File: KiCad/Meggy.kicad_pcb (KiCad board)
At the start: 4 copper layers, 17.4 x 54 mm, 19 parts, among them J1 USB_B_Micro, J2 Conn_01x03, Q1 DMP2305U-7, Q2 DMP2305U-7, U1 ROM-socket-42pin, U2 AT90USB1286-MU, U3 M29F160F, X1 Standard_Clock_Oscillators_XT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

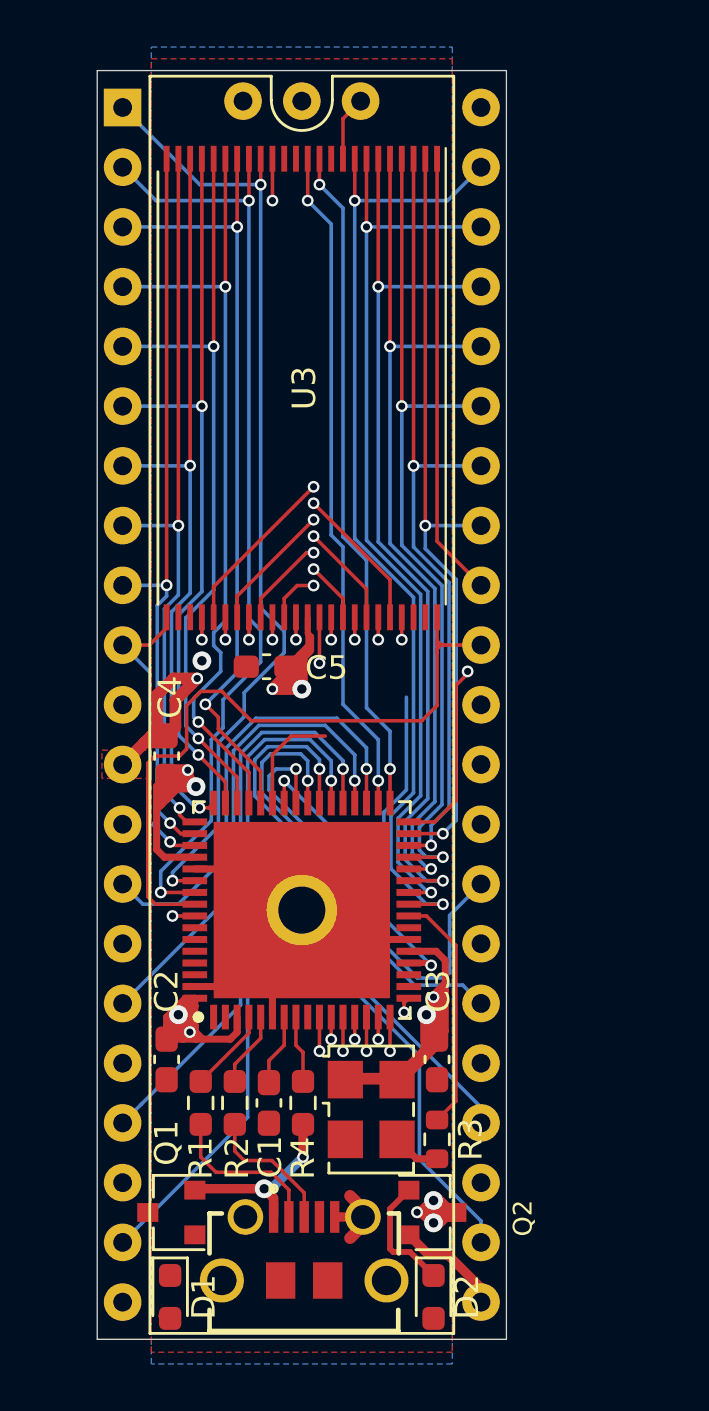
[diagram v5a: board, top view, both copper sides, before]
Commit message: Add circuit for controlling Flash-OE signal
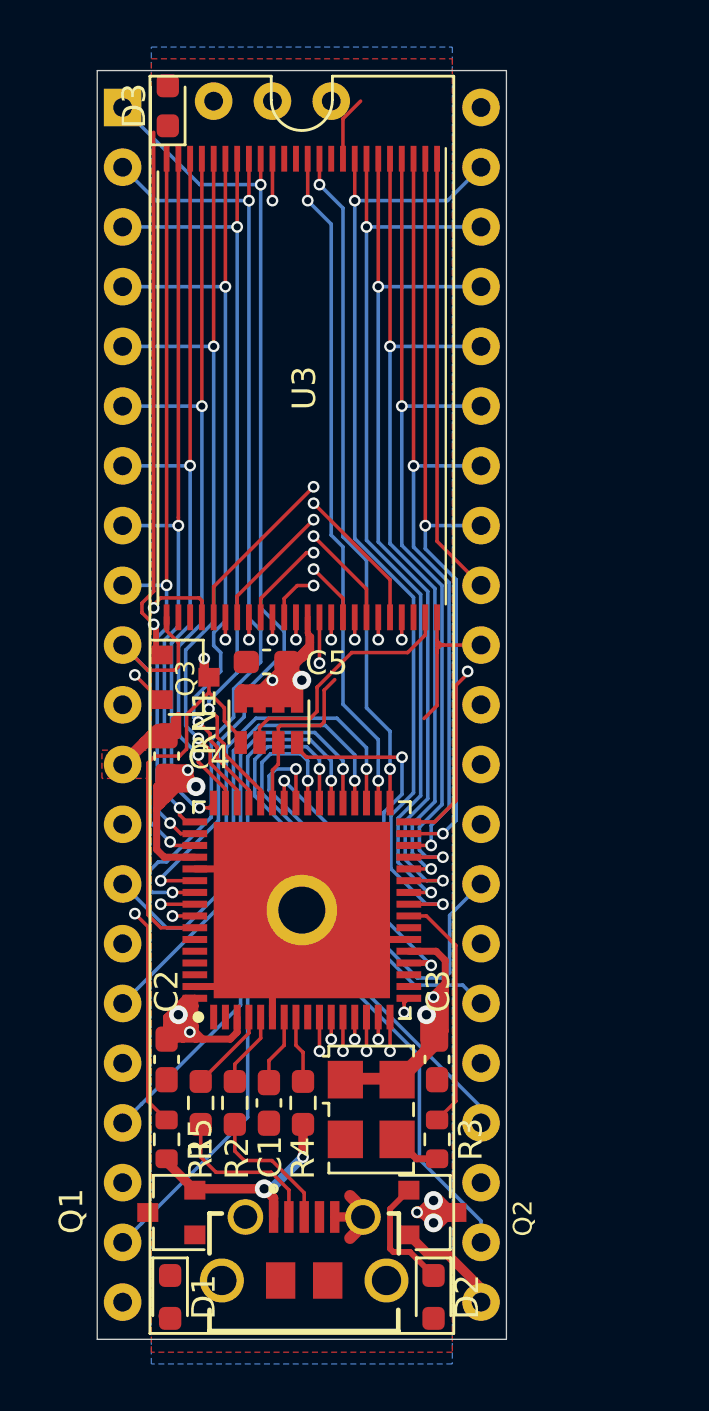
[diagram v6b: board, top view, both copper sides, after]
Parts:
- added D3: MMDL6050T1G, Meggy:D_0603_1608Metric_Pad_0.975x0.95mm_HandSolder, F.Cu at (126.3, 58.8)
- added Q3: DMP2305U-7, Package_TO_SOT_SMD:SOT-23, F.Cu at (127.0, 83.1)
- added R5: 10k, Resistor_SMD:R_0603_1608Metric, F.Cu at (126.2, 102.8)
- added RN1: 10k, Meggy:RESCAF80P320X160X60-8N, F.Cu at (130.6, 85.0)
- moved J2 1.25 mm to (130.8, 58.6)
- moved C5 0.20 mm to (130.5, 82.5)
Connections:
- net Net-(C1-Pad1) renamed /UCAP
- U2 pad 58: PF3 -> OE_FLASH
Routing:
- net Net-(D3-Pad1): track 0.00 -> 45.1 mm, vias 0 -> 2
- net OE_FLASH: track 0.95 -> 24.3 mm, vias 1 -> 2
- net BYTE: track 0.00 -> 10.7 mm
- net BOARD_5V: track 72.6 -> 81.9 mm
- net OE_SOCKET: track 0.00 -> 9.23 mm, vias 0 -> 1
- net GND: track 35.0 -> 31.1 mm, vias 2 -> 0
- net A0: track 12.9 -> 15.8 mm
- net HWB: track 4.63 -> 7.35 mm
- net RESET: track 13.6 -> 15.8 mm, vias 1 -> 2
- net VBUS_5V: track 7.73 -> 9.57 mm
- net D0: track 41.5 -> 43.0 mm
- net A17: track 40.6 -> 41.4 mm
- net A18: track 41.3 -> 42.0 mm
- net A16: track 29.6 -> 29.3 mm, vias 0 -> 1

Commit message: Add 10k pull-up resistor network for RY-BY, WE, RST and A19 signals
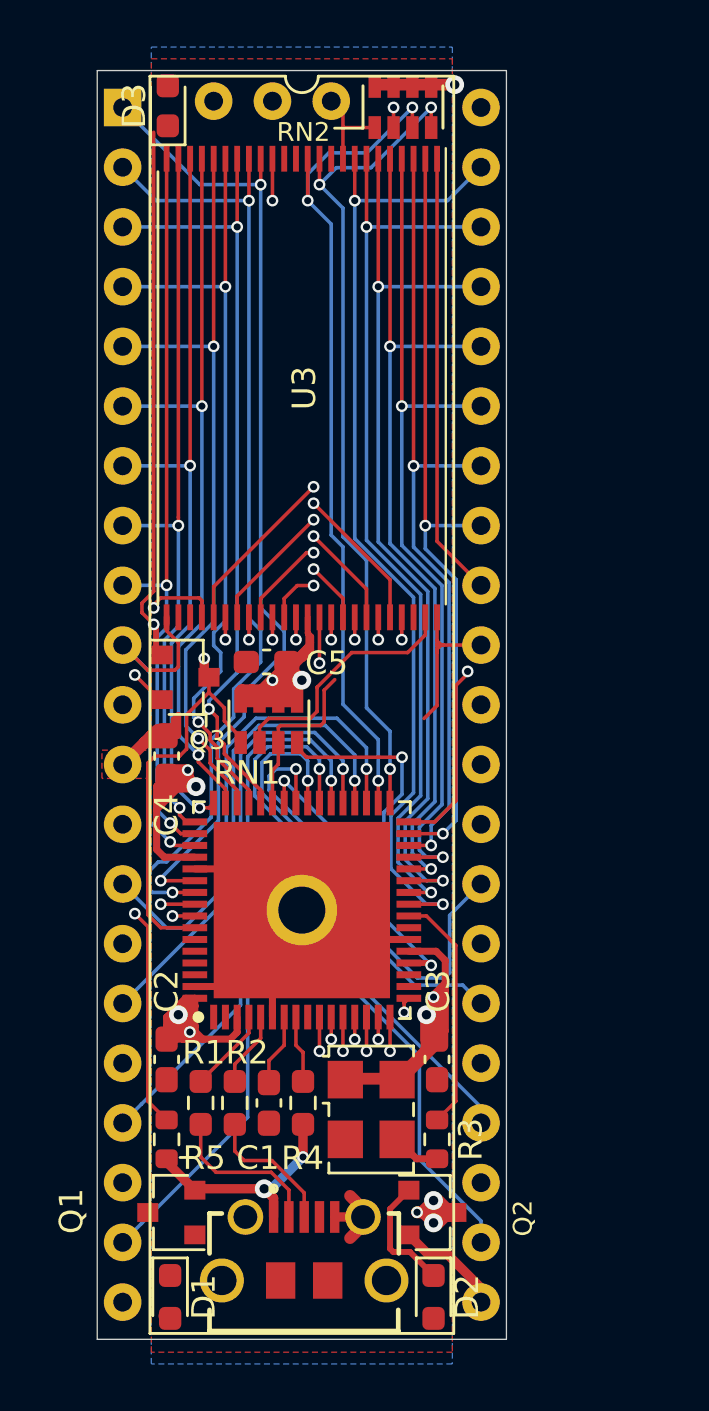
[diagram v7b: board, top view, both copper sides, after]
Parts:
- added RN2: 10k, Meggy:RESCAF80P320X160X60-8N, F.Cu at (136.3, 58.9)
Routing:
- net RY-BY: track 35.5 -> 43.1 mm, vias 2 -> 3
- net RST: track 28.6 -> 36.2 mm, vias 2 -> 3
- net WE: track 28.6 -> 35.6 mm, vias 2 -> 3
- net BOARD_5V: track 81.9 -> 85.4 mm, vias 11 -> 12
- net A19: track 2.76 -> 4.02 mm

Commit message: Fix footprint for diode D3 and silkscreen fixes
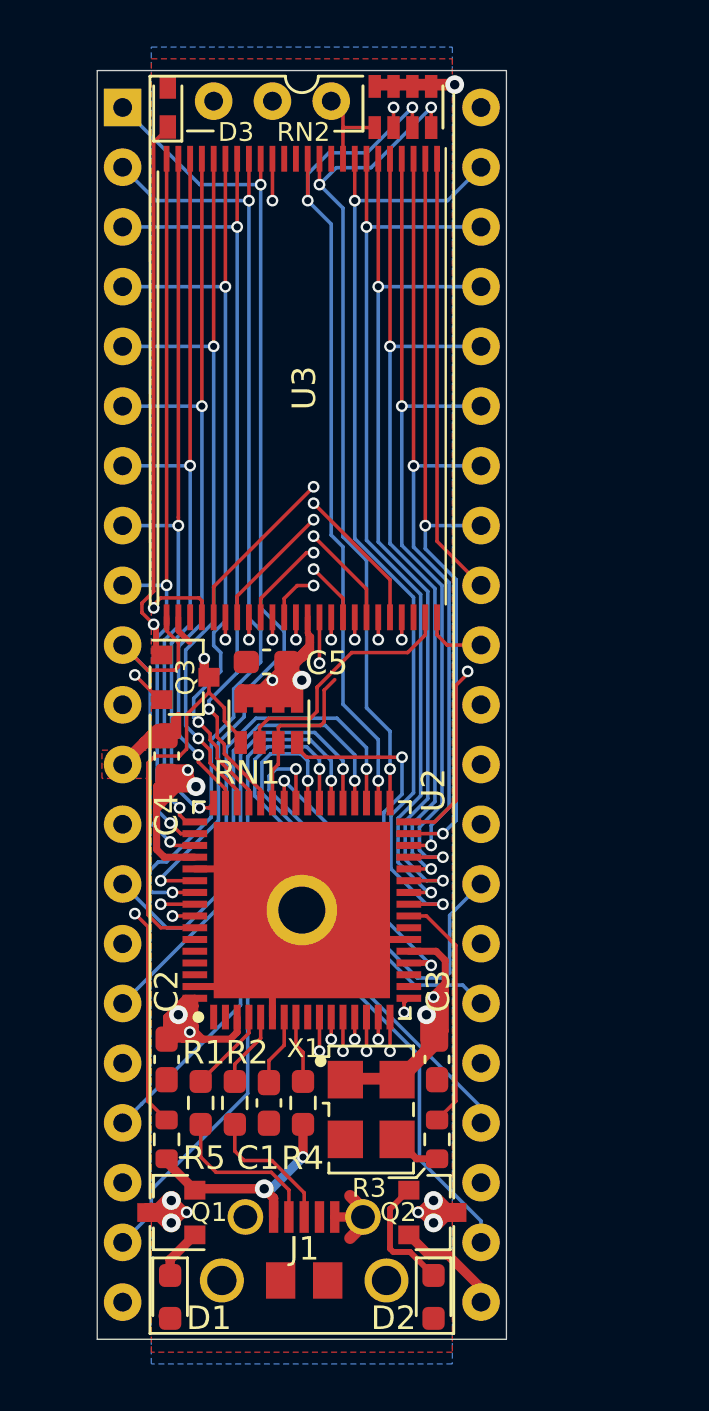
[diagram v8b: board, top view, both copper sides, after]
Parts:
- D3: footprint Meggy:D_0603_1608Metric_Pad_0.975x0.95mm_HandSolder -> Diode_SMD:D_SOD-523
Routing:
- net BOARD_5V: track 85.4 -> 90.3 mm, vias 12 -> 15
- net A16: track 29.3 -> 24.9 mm
- net Net-(D1-Pad1): track 0.00 -> 2.16 mm
- net GND: track 31.1 -> 32.3 mm
